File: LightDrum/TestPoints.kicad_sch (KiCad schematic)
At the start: 3 parts

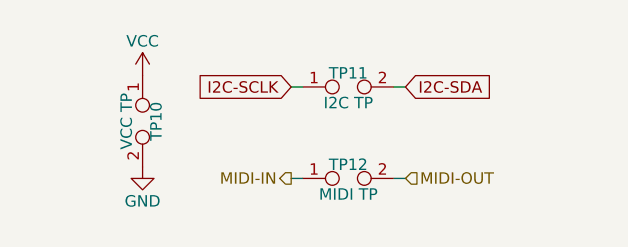
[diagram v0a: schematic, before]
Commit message: Replace interface harnesses with FPC cable
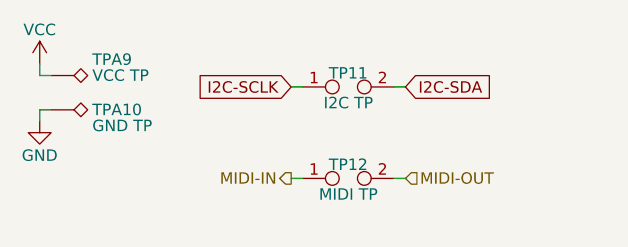
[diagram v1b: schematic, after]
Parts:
- removed TP10: VCC TP, Connector_PinHeader_2.54mm:PinHeader_1x02_P2.54mm_Vertical, symbol Connector:TestPoint_2Pole
- added TPA10: GND TP, TestPoint:TestPoint_Loop_D2.54mm_Drill1.5mm_Beaded, symbol Connector:TestPoint_Alt
- added TPA9: VCC TP, TestPoint:TestPoint_Loop_D2.54mm_Drill1.5mm_Beaded, symbol Connector:TestPoint_Alt
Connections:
- net GND: now also TPA10.1
- net VCC: now also TPA9.1
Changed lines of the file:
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@@
 (kicad_sch (version 20211123) (generator eeschema)
   (paper "A4")
+  (wire (pts (xy 24.13 25.4) (xy 22.86 25.4))
+    (stroke (width 0) (type default) (color 0 0 0 0))
+  )
   (wire (pts (xy 50.8 36.83) (xy 52.07 36.83))
     (stroke (width 0) (type default) (color 0 0 0 0))
@@
     (stroke (width 0) (type default) (color 0 0 0 0))
   )
+  (wire (pts (xy 24.13 29.21) (xy 22.86 29.21))
+    (stroke (width 0) (type default) (color 0 0 0 0))
+  )
   (wire (pts (xy 50.8 26.67) (xy 52.07 26.67))
+    (stroke (width 0) (type default) (color 0 0 0 0))
+  )
+  (wire (pts (xy 22.86 29.21) (xy 22.86 30.48))
+    (stroke (width 0) (type default) (color 0 0 0 0))
+  )
+  (wire (pts (xy 22.86 25.4) (xy 22.86 24.13))
     (stroke (width 0) (type default) (color 0 0 0 0))
   )
@@
     (pin "2")
   )
-  (symbol (lib_id "power:GND") (at 34.29 35.56 0) (unit 1)
+  (symbol (lib_id "power:GND") (at 22.86 30.48 0) (unit 1)
     (in_bom yes) (on_board yes)
-    (property "Reference" "#PWR0120" (id 0) (at 34.29 41.91 0)
+    (property "Reference" "#PWR0120" (id 0) (at 22.86 36.83 0)
       (effects (font (size 1.27 1.27)) hide)
     )
-    (property "Value" "GND" (id 1) (at 34.29 39.37 0))
-    (property "Footprint" "" (id 2) (at 34.29 35.56 0)
+    (property "Value" "GND" (id 1) (at 22.86 34.29 0))
+    (property "Footprint" "" (id 2) (at 22.86 30.48 0)
       (effects (font (size 1.27 1.27)) hide)
     )
-    (property "Datasheet" "" (id 3) (at 34.29 35.56 0)
+    (property "Datasheet" "" (id 3) (at 22.86 30.48 0)
       (effects (font (size 1.27 1.27)) hide)
     )
     (pin "1")
   )
-  (symbol (lib_id "power:VCC") (at 34.29 25.4 0) (unit 1)
+  (symbol (lib_id "power:VCC") (at 22.86 24.13 0) (unit 1)
     (in_bom yes) (on_board yes)
-    (property "Reference" "#PWR0121" (id 0) (at 34.29 29.21 0)
+    (property "Reference" "#PWR0121" (id 0) (at 22.86 27.94 0)
       (effects (font (size 1.27 1.27)) hide)
     )
-    (property "Value" "VCC" (id 1) (at 34.29 21.59 0))
-    (property "Footprint" "" (id 2) (at 34.29 25.4 0)
+    (property "Value" "VCC" (id 1) (at 22.86 20.32 0))
+    (property "Footprint" "" (id 2) (at 22.86 24.13 0)
       (effects (font (size 1.27 1.27)) hide)
     )
-    (property "Datasheet" "" (id 3) (at 34.29 25.4 0)
+    (property "Datasheet" "" (id 3) (at 22.86 24.13 0)
       (effects (font (size 1.27 1.27)) hide)
     )
     (pin "1")
   )
-  (symbol (lib_id "Connector:TestPoint_2Pole") (at 34.29 30.48 270) (unit 1)
+  (symbol (lib_id "Connector:TestPoint_Alt") (at 24.13 29.21 270) (unit 1)
     (in_bom yes) (on_board yes)
-    (property "Reference" "TP10" (id 0) (at 35.814 30.48 0))
-    (property "Value" "VCC TP" (id 1) (at 32.512 30.48 0))
-    (property "Footprint" "Connector_PinHeader_2.54mm:PinHeader_1x02_P2.54mm_Vertical" (id 2) (at 34.29 30.48 0)
+    (property "Reference" "TPA10" (id 0) (at 28.702 29.21 90)
+      (effects (font (size 1.27 1.27)) (justify left))
+    )
+    (property "Value" "GND TP" (id 1) (at 28.702 30.988 90)
+      (effects (font (size 1.27 1.27)) (justify left))
+    )
+    (property "Footprint" "TestPoint:TestPoint_Loop_D2.54mm_Drill1.5mm_Beaded" (id 2) (at 24.13 34.29 0)
       (effects (font (size 1.27 1.27)) hide)
     )
-    (property "Datasheet" "~" (id 3) (at 34.29 30.48 0)
+    (property "Datasheet" "~" (id 3) (at 24.13 34.29 0)
       (effects (font (size 1.27 1.27)) hide)
     )
     (pin "1")
-    (pin "2")
+  )
+  (symbol (lib_id "Connector:TestPoint_Alt") (at 24.13 25.4 270) (unit 1)
+    (in_bom yes) (on_board yes)
+    (property "Reference" "TPA9" (id 0) (at 28.702 23.622 90)
+      (effects (font (size 1.27 1.27)) (justify left))
+    )
+    (property "Value" "VCC TP" (id 1) (at 28.702 25.4 90)
+      (effects (font (size 1.27 1.27)) (justify left))
+    )
+    (property "Footprint" "TestPoint:TestPoint_Loop_D2.54mm_Drill1.5mm_Beaded" (id 2) (at 24.13 30.48 0)
+      (effects (font (size 1.27 1.27)) hide)
+    )
+    (property "Datasheet" "~" (id 3) (at 24.13 30.48 0)
+      (effects (font (size 1.27 1.27)) hide)
+    )
+    (pin "1")
   )
 )

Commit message: Add docs and gerbers for REV7
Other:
- company: (none) -> Daxxn Industries
- title: (none) -> LightDrum
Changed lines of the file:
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@@
 (kicad_sch (version 20211123) (generator eeschema)
   (paper "A4")
+  (title_block
+    (title "LightDrum")
+    (rev "REV7")
+    (company "Daxxn Industries")
+  )
   (wire (pts (xy 24.13 25.4) (xy 22.86 25.4))
     (stroke (width 0) (type default) (color 0 0 0 0))

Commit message: General component placement
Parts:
- renumbered TP11 to TP1101, TP12 to TP1102, TPA9 to TPA1101, TPA10 to TPA1102
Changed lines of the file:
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@@
   (symbol (lib_id "Connector:TestPoint_2Pole") (at 57.15 26.67 0) (unit 1)
     (in_bom yes) (on_board yes)
-    (property "Reference" "TP11" (id 0) (at 57.15 25.146 0))
+    (property "Reference" "TP1101" (id 0) (at 57.15 25.146 0))
     (property "Value" "I2C TP" (id 1) (at 57.15 28.448 0))
     (property "Footprint" "Connector_PinHeader_2.54mm:PinHeader_1x02_P2.54mm_Vertical" (id 2) (at 57.15 26.67 0)
@@
   (symbol (lib_id "Connector:TestPoint_2Pole") (at 57.15 36.83 0) (unit 1)
     (in_bom yes) (on_board yes)
-    (property "Reference" "TP12" (id 0) (at 57.15 35.306 0))
+    (property "Reference" "TP1102" (id 0) (at 57.15 35.306 0))
     (property "Value" "MIDI TP" (id 1) (at 57.15 38.608 0))
     (property "Footprint" "Connector_PinHeader_2.54mm:PinHeader_1x02_P2.54mm_Vertical" (id 2) (at 57.15 36.83 0)
@@
   (symbol (lib_id "power:GND") (at 22.86 30.48 0) (unit 1)
     (in_bom yes) (on_board yes)
-    (property "Reference" "#PWR0120" (id 0) (at 22.86 36.83 0)
+    (property "Reference" "#PWR01102" (id 0) (at 22.86 36.83 0)
       (effects (font (size 1.27 1.27)) hide)
     )
@@
   (symbol (lib_id "power:VCC") (at 22.86 24.13 0) (unit 1)
     (in_bom yes) (on_board yes)
-    (property "Reference" "#PWR0121" (id 0) (at 22.86 27.94 0)
+    (property "Reference" "#PWR01101" (id 0) (at 22.86 27.94 0)
       (effects (font (size 1.27 1.27)) hide)
     )
@@
   (symbol (lib_id "Connector:TestPoint_Alt") (at 24.13 29.21 270) (unit 1)
     (in_bom yes) (on_board yes)
-    (property "Reference" "TPA10" (id 0) (at 28.702 29.21 90)
+    (property "Reference" "TPA1102" (id 0) (at 28.702 29.21 90)
       (effects (font (size 1.27 1.27)) (justify left))
     )
@@
   (symbol (lib_id "Connector:TestPoint_Alt") (at 24.13 25.4 270) (unit 1)
     (in_bom yes) (on_board yes)
-    (property "Reference" "TPA9" (id 0) (at 28.702 23.622 90)
+    (property "Reference" "TPA1101" (id 0) (at 28.702 23.622 90)
       (effects (font (size 1.27 1.27)) (justify left))
     )

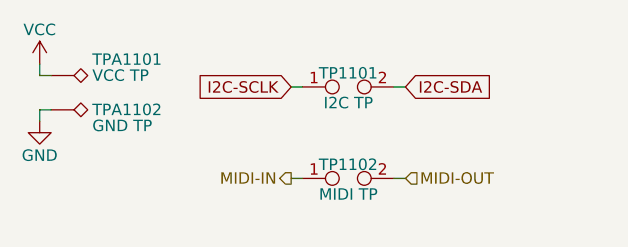
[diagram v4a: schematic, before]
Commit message: Replace barrel jacks with proper DIN4 conn and more
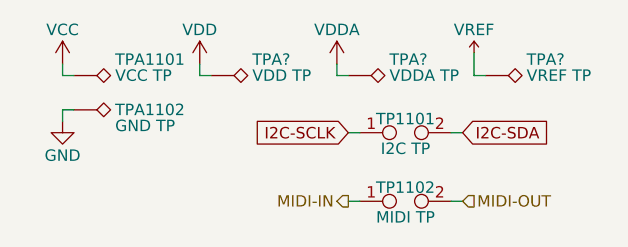
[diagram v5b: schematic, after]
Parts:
- added TPA?: VDD TP, TestPoint:TestPoint_Loop_D2.54mm_Drill1.5mm_Beaded, symbol Connector:TestPoint_Alt
- added TPA?: VREF TP, TestPoint:TestPoint_Loop_D2.54mm_Drill1.5mm_Beaded, symbol Connector:TestPoint_Alt
- added TPA?: VDDA TP, TestPoint:TestPoint_Loop_D2.54mm_Drill1.5mm_Beaded, symbol Connector:TestPoint_Alt
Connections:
- new net VDD: TPA?.1
- new net VDDA: TPA?.1
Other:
- moved on the sheet: TP1101, TP1102, TPA1101, TPA1102

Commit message: Replace old MOSFETs with a more compact package
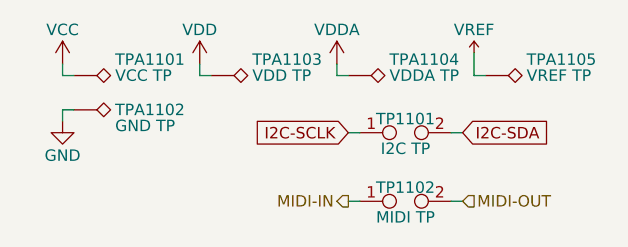
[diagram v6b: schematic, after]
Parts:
- gave numbers to parts that had none: 3
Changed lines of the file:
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@@
   (symbol (lib_id "Daxxn_Power:VREF") (at 71.12 22.86 0) (unit 1)
     (in_bom no) (on_board no)
-    (property "Reference" "+5UF?" (id 0) (at 71.12 17.78 0)
+    (property "Reference" "#+5UF01101" (id 0) (at 71.12 17.78 0)
       (effects (font (size 1.27 1.27)) hide)
     )
@@
   (symbol (lib_id "Connector:TestPoint_Alt") (at 41.91 25.4 270) (unit 1)
     (in_bom yes) (on_board yes)
-    (property "Reference" "TPA?" (id 0) (at 46.482 23.622 90)
+    (property "Reference" "TPA1103" (id 0) (at 46.482 23.622 90)
       (effects (font (size 1.27 1.27)) (justify left))
     )
@@
   (symbol (lib_id "power:VCC") (at 25.4 24.13 0) (unit 1)
     (in_bom yes) (on_board yes)
-    (property "Reference" "#PWR?" (id 0) (at 25.4 27.94 0)
+    (property "Reference" "#PWR01101" (id 0) (at 25.4 27.94 0)
       (effects (font (size 1.27 1.27)) hide)
     )
@@
   (symbol (lib_id "power:VDD") (at 40.64 24.13 0) (unit 1)
     (in_bom yes) (on_board yes)
-    (property "Reference" "#PWR?" (id 0) (at 40.64 27.94 0)
+    (property "Reference" "#PWR01103" (id 0) (at 40.64 27.94 0)
       (effects (font (size 1.27 1.27)) hide)
     )
@@
   (symbol (lib_id "Connector:TestPoint_Alt") (at 72.39 25.4 270) (unit 1)
     (in_bom yes) (on_board yes)
-    (property "Reference" "TPA?" (id 0) (at 76.962 23.622 90)
+    (property "Reference" "TPA1105" (id 0) (at 76.962 23.622 90)
       (effects (font (size 1.27 1.27)) (justify left))
     )
@@
   (symbol (lib_id "Connector:TestPoint_Alt") (at 57.15 25.4 270) (unit 1)
     (in_bom yes) (on_board yes)
-    (property "Reference" "TPA?" (id 0) (at 61.722 23.622 90)
+    (property "Reference" "TPA1104" (id 0) (at 61.722 23.622 90)
       (effects (font (size 1.27 1.27)) (justify left))
     )
@@
   (symbol (lib_id "power:VDDA") (at 55.88 24.13 0) (unit 1)
     (in_bom yes) (on_board yes)
-    (property "Reference" "#PWR?" (id 0) (at 55.88 27.94 0)
+    (property "Reference" "#PWR01104" (id 0) (at 55.88 27.94 0)
       (effects (font (size 1.27 1.27)) hide)
     )

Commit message: Lock REV8 Layout and send to PCB MNF
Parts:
- removed TPA1105: VREF TP, TestPoint:TestPoint_Loop_D2.54mm_Drill1.5mm_Beaded, symbol Connector:TestPoint_Alt
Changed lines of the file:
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@@
-    (stroke (width 0) (type default) (color 0 0 0 0))
-  )
-  (wire (pts (xy 71.12 25.4) (xy 71.12 22.86))
     (stroke (width 0) (type default) (color 0 0 0 0))
   )
   (wire (pts (xy 57.15 25.4) (xy 55.88 25.4))
-    (stroke (width 0) (type default) (color 0 0 0 0))
-  )
-  (wire (pts (xy 72.39 25.4) (xy 71.12 25.4))
     (stroke (width 0) (type default) (color 0 0 0 0))
   )
@@
   (hierarchical_label "MIDI-IN" (shape output) (at 57.15 39.37 180)
     (effects (font (size 1.27 1.27)) (justify right))
-  )
-  (symbol (lib_id "Daxxn_Power:VREF") (at 71.12 22.86 0) (unit 1)
-    (in_bom no) (on_board no)
-    (property "Reference" "#+5UF01101" (id 0) (at 71.12 17.78 0)
-      (effects (font (size 1.27 1.27)) hide)
-    )
-    (property "Value" "VREF" (id 1) (at 71.12 20.32 0))
-    (property "Footprint" "" (id 2) (at 71.12 22.86 0)
-      (effects (font (size 1.27 1.27)) hide)
-    )
-    (property "Datasheet" "" (id 3) (at 71.12 22.86 0)
-      (effects (font (size 1.27 1.27)) hide)
-    )
-    (pin "1")
   )
   (symbol (lib_id "Connector:TestPoint_2Pole") (at 63.5 31.75 0) (unit 1)
@@
       (effects (font (size 1.27 1.27)) hide)
     )
-    (pin "1")
-  )
-  (symbol (lib_id "Connector:TestPoint_Alt") (at 72.39 25.4 270) (unit 1)
-    (in_bom yes) (on_board yes)
-    (property "Reference" "TPA1105" (id 0) (at 76.962 23.622 90)
-      (effects (font (size 1.27 1.27)) (justify left))
-    )
-    (property "Value" "VREF TP" (id 1) (at 76.962 25.4 90)
-      (effects (font (size 1.27 1.27)) (justify left))
-    )
-    (property "Footprint" "TestPoint:TestPoint_Loop_D2.54mm_Drill1.5mm_Beaded" (id 2) (at 72.39 30.48 0)
-      (effects (font (size 1.27 1.27)) hide)
-    )
-    (property "Datasheet" "~" (id 3) (at 72.39 30.48 0)
-      (effects (font (size 1.27 1.27)) hide)
-    )
